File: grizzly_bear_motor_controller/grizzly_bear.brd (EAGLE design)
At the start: 71 x 38.9 mm, 56 parts, among them Q1 PH7030L, Q2 PH7030L, Q3 PH7030L, Q4 PH7030L, Q5 FDD4141TO252, U1 A4940, U2 ATMEGA32U4-AU, U3 ACS714, U4 UA78L00, Y1 16MHz

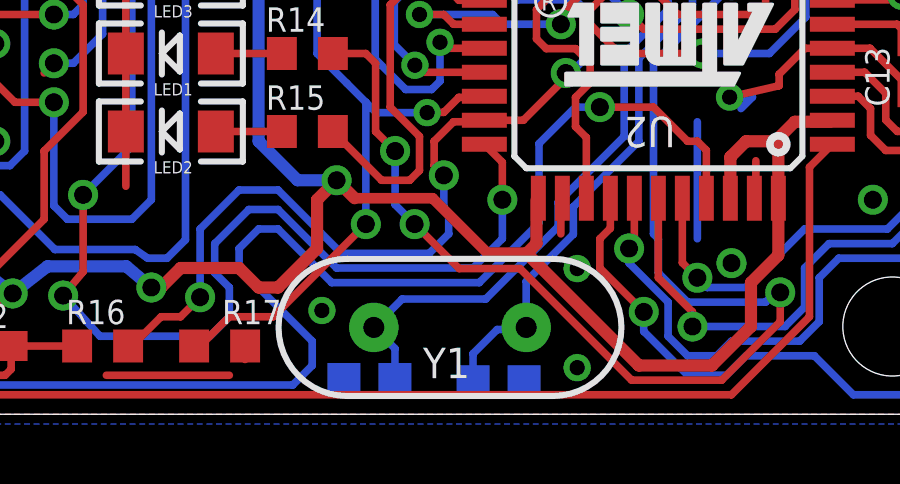
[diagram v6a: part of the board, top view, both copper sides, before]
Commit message: Expand drill holes of crystal
Change-Id: Ic247b6292cbf41966bf56fa91863cb11911d346f
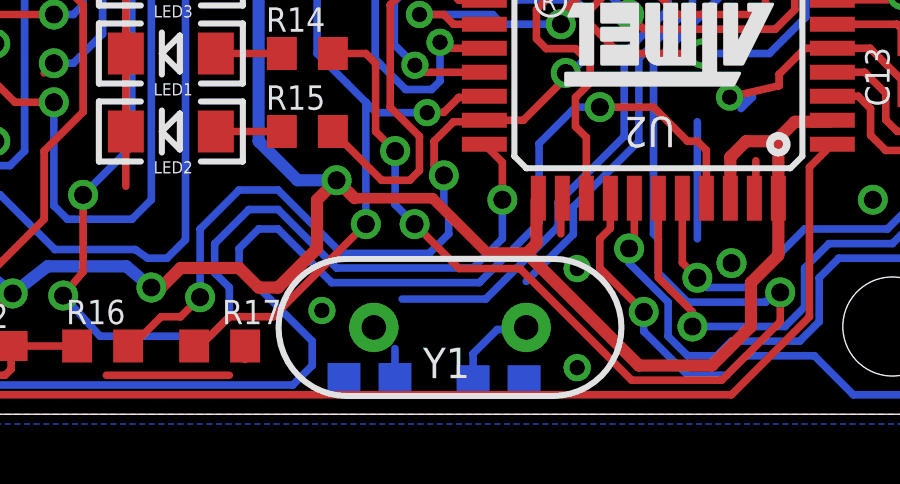
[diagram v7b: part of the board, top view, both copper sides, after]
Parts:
- Y1: device SparkFun-FreqCtrl:HC49US -> pie:HC49US
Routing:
- net N$26: track 23.7 -> 21.4 mm
- net N$27: track 21.7 -> 20.1 mm
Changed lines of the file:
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@@
 <layer number="27" name="tValues" color="7" fill="1" visible="no" active="yes"/>
 <layer number="28" name="bValues" color="12" fill="1" visible="no" active="yes"/>
-<layer number="29" name="tStop" color="7" fill="3" visible="no" active="yes"/>
-<layer number="30" name="bStop" color="7" fill="6" visible="no" active="yes"/>
+<layer number="29" name="tStop" color="7" fill="3" visible="yes" active="yes"/>
+<layer number="30" name="bStop" color="7" fill="6" visible="yes" active="yes"/>
 <layer number="31" name="tCream" color="7" fill="4" visible="no" active="yes"/>
 <layer number="32" name="bCream" color="7" fill="5" visible="no" active="yes"/>
@@
 <attribute name="VALUE" x="53.493496875" y="0.443" size="0.6096" layer="28" font="vector" ratio="15" rot="MR0"/>
 </element>
-<element name="Y1" library="SparkFun-FreqCtrl" package="HC49US" value="16MHz" x="52.53" y="1.594996875" smashed="yes" rot="R180">
-<attribute name="VALUE" x="52.41" y="3.256996875" size="0.8128" layer="27" font="vector" ratio="15" rot="R180" align="bottom-center"/>
-<attribute name="NAME" x="52.41" y="-0.097003125" size="1.016" layer="25" font="vector" ratio="15" rot="R180" align="top-center"/>
-</element>
 <element name="JP4" library="SparkFun-Connectors" package="MOLEX-1X3" value="" x="52.325003125" y="34.775" rot="R180"/>
 <element name="JP3" library="SparkFun-Connectors" package="MOLEX-1X4" value="" x="44.2" y="34.775" rot="R180"/>
@@
 <attribute name="NAME" x="23.695" y="26.555" size="1.27" layer="25" font="vector" ratio="15" align="top-center"/>
 <attribute name="VALUE" x="24.995" y="30.365" size="0.4064" layer="27" rot="R180"/>
+</element>
+<element name="Y1" library="pie" package="HC49US" value="16MHz" x="52.53" y="1.594996875" smashed="yes" rot="R180">
+<attribute name="VALUE" x="57.61" y="5.531996875" size="1.27" layer="27" ratio="10" rot="R180"/>
+<attribute name="NAME" x="52.41" y="-0.097003125" size="1.016" layer="25" font="vector" ratio="15" align="bottom-center"/>
 </element>
 </elements>
@@
 <signal name="N$26">
 <contactref element="C14" pad="2"/>
-<contactref element="Y1" pad="2"/>
 <contactref element="U2" pad="17"/>
 <via x="59.475003125" y="13.8125" extent="1-16" drill="0.6"/>
@@
 <wire x1="58.337503125" y1="7.9625" x2="56.134" y2="5.758996875" width="0.254" layer="16"/>
 <wire x1="59.47500625" y1="13.812503125" x2="59.475003125" y2="13.8125" width="0.254" layer="1"/>
-<wire x1="50.935003125" y1="2.54" x2="49.99" y2="1.594996875" width="0.254" layer="16"/>
 <wire x1="50.935003125" y1="2.54" x2="53.721" y2="2.54" width="0.254" layer="16"/>
 <wire x1="53.721" y1="2.54" x2="56.134" y2="4.953" width="0.254" layer="16"/>
@@
 <wire x1="59.800003125" y1="13.4875" x2="59.475003125" y2="13.8125" width="0.254" layer="16"/>
 <wire x1="50.695" y1="-0.091003125" x2="50.695" y2="0.889996875" width="0.254" layer="16"/>
-<wire x1="50.695" y1="0.889996875" x2="49.99" y2="1.594996875" width="0.254" layer="16"/>
+<contactref element="Y1" pad="2"/>
+<wire x1="49.99" y1="1.594996875" x2="50.935003125" y2="2.54" width="0" layer="19" extent="16-16"/>
+<wire x1="50.695" y1="0.889996875" x2="49.99" y2="1.594996875" width="0" layer="19" extent="16-16"/>
 </signal>
 <signal name="N$27">
 <contactref element="C15" pad="2"/>
-<contactref element="Y1" pad="1"/>
 <contactref element="U2" pad="16"/>
 <wire x1="58.825003125" y1="10.5625" x2="60.612503125" y2="12.35" width="0.254" layer="16"/>
@@
 <wire x1="60.27500625" y1="17.5" x2="60.27500625" y2="17.825" width="0.254" layer="1"/>
 <wire x1="60.27500625" y1="17.825" x2="60.287503125" y2="17.837496875" width="0.254" layer="1"/>
-<wire x1="55.07" y1="1.594996875" x2="55.07" y2="3.127" width="0.254" layer="16"/>
 <wire x1="55.07" y1="3.127" x2="56.642" y2="4.699" width="0.254" layer="16"/>
 <wire x1="56.642" y1="4.699" x2="56.642" y2="5.616996875" width="0.254" layer="16"/>
@@
 <wire x1="53.299" y1="0.721" x2="54.102" y2="1.524" width="0.254" layer="16"/>
 <wire x1="54.102" y1="1.524" x2="54.999003125" y2="1.524" width="0.254" layer="16"/>
-<wire x1="54.999003125" y1="1.524" x2="55.07" y2="1.594996875" width="0.254" layer="16"/>
+<contactref element="Y1" pad="1"/>
+<wire x1="55.07" y1="1.594996875" x2="55.07" y2="3.127" width="0" layer="19" extent="16-16"/>
+<wire x1="54.999003125" y1="1.524" x2="55.07" y2="1.594996875" width="0" layer="19" extent="16-16"/>
 </signal>
 <signal name="N$16">

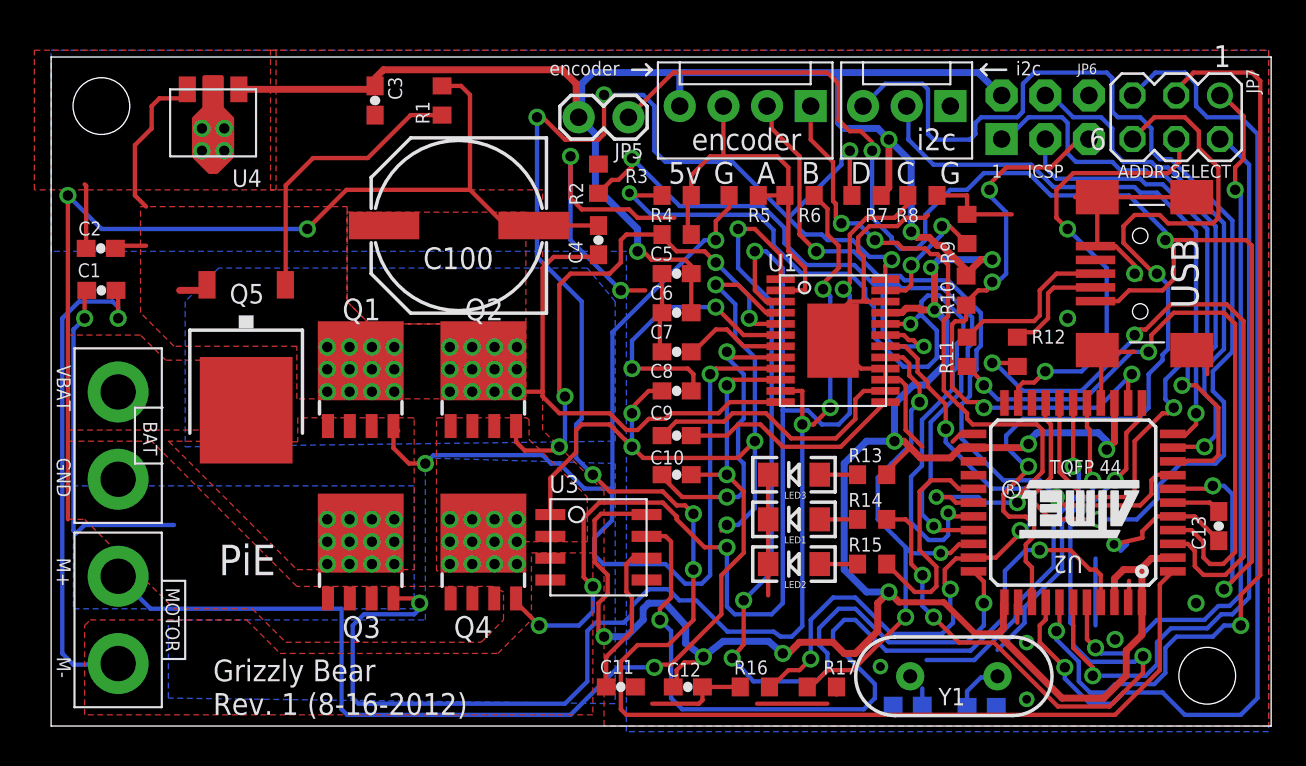
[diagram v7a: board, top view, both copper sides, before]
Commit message: Make almost all 0603 passives the same direction
Change-Id: I208b639b8e92d3f30c2154f669f06853ede68341
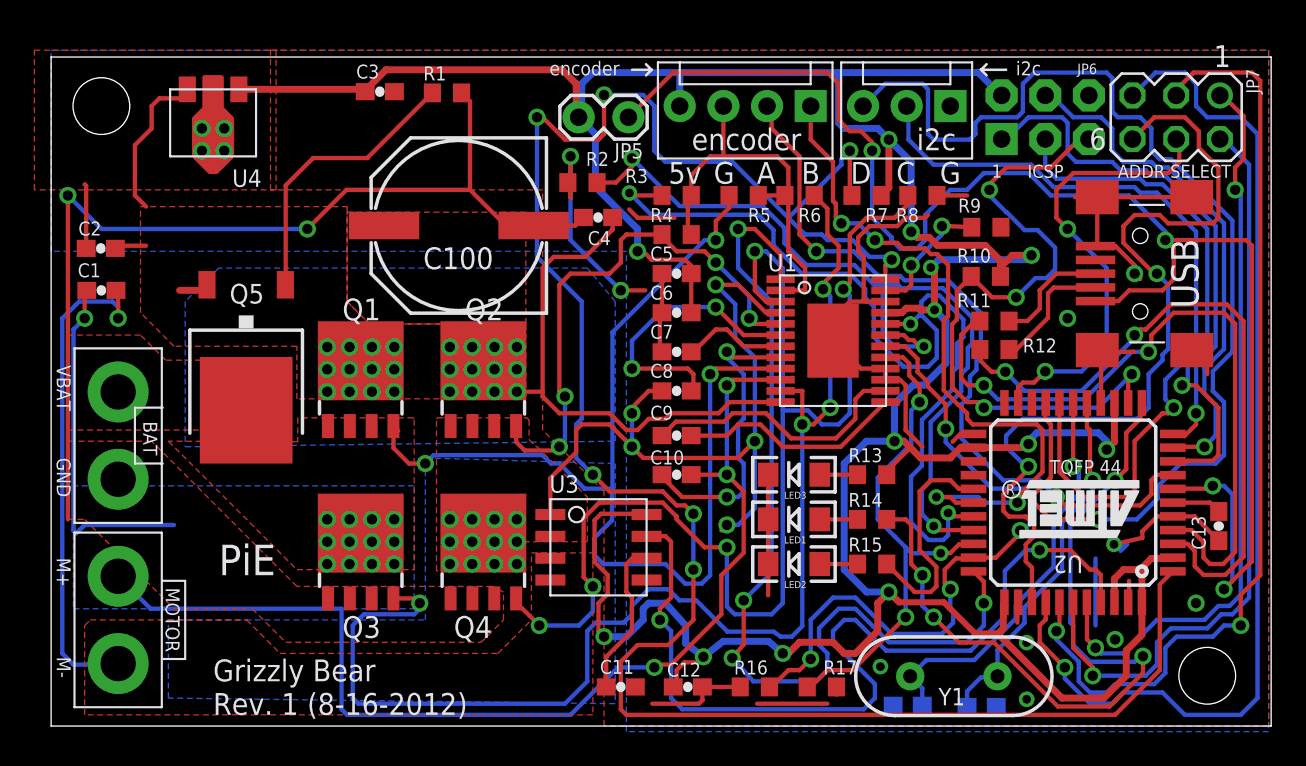
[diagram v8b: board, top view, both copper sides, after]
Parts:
- moved R11 2.40 mm to (54.9, 22.3), turned to 180 degrees
- moved R10 1.41 mm to (54.4, 24.9), turned to 180 degrees
- moved R12 1.34 mm to (54.9, 20.6), turned to 180 degrees
- moved C4 1.32 mm to (31.8, 28.3), turned to 0 degrees
- moved R9 1.13 mm to (54.4, 27.7), turned to 0 degrees
- moved R2 0.96 mm to (30.9, 30.3), turned to 180 degrees
- moved C3 0.58 mm to (19.1, 35.6), turned to 0 degrees
- moved R1 0.53 mm to (23.0, 35.5), turned to 180 degrees
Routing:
- net GND: track 140.8 -> 133.4 mm
- net RESET: track 35.2 -> 40.8 mm
- net 5V: track 208.8 -> 213.6 mm
- net N$9: track 38.0 -> 41.9 mm
- net N$24: track 9.86 -> 6.81 mm
- net N$26: track 21.4 -> 23.7 mm
- net BATGND: track 59.7 -> 57.5 mm
- net VBAT: track 40.8 -> 42.9 mm
- net N$27: track 20.1 -> 21.7 mm
- net N$29: track 6.61 -> 7.37 mm
